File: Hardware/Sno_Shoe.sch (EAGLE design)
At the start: 39 parts, among them J1 QWIIC_RIGHT_ANGLE, J2 MOLEX_HDMI_208658-1051, U1 CH340E

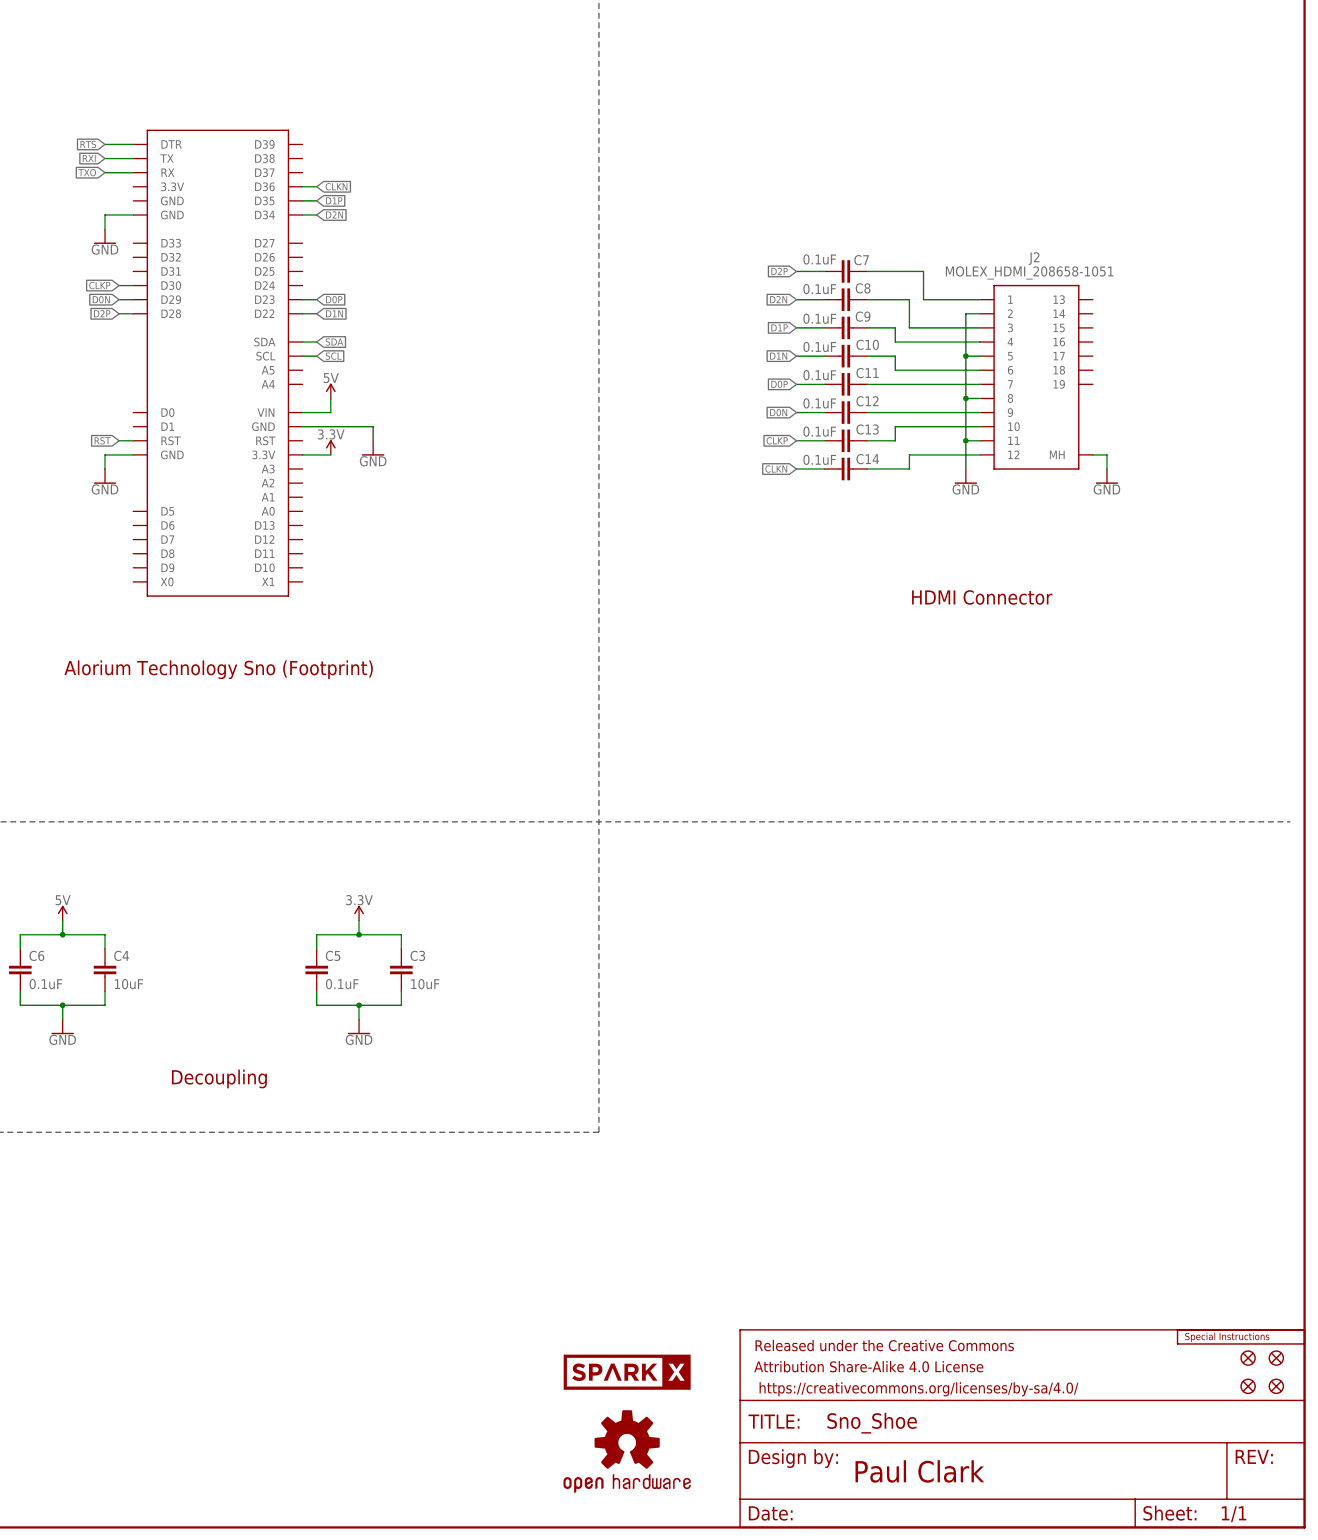
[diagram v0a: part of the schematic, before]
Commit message: Changed the HDMI connector footprint
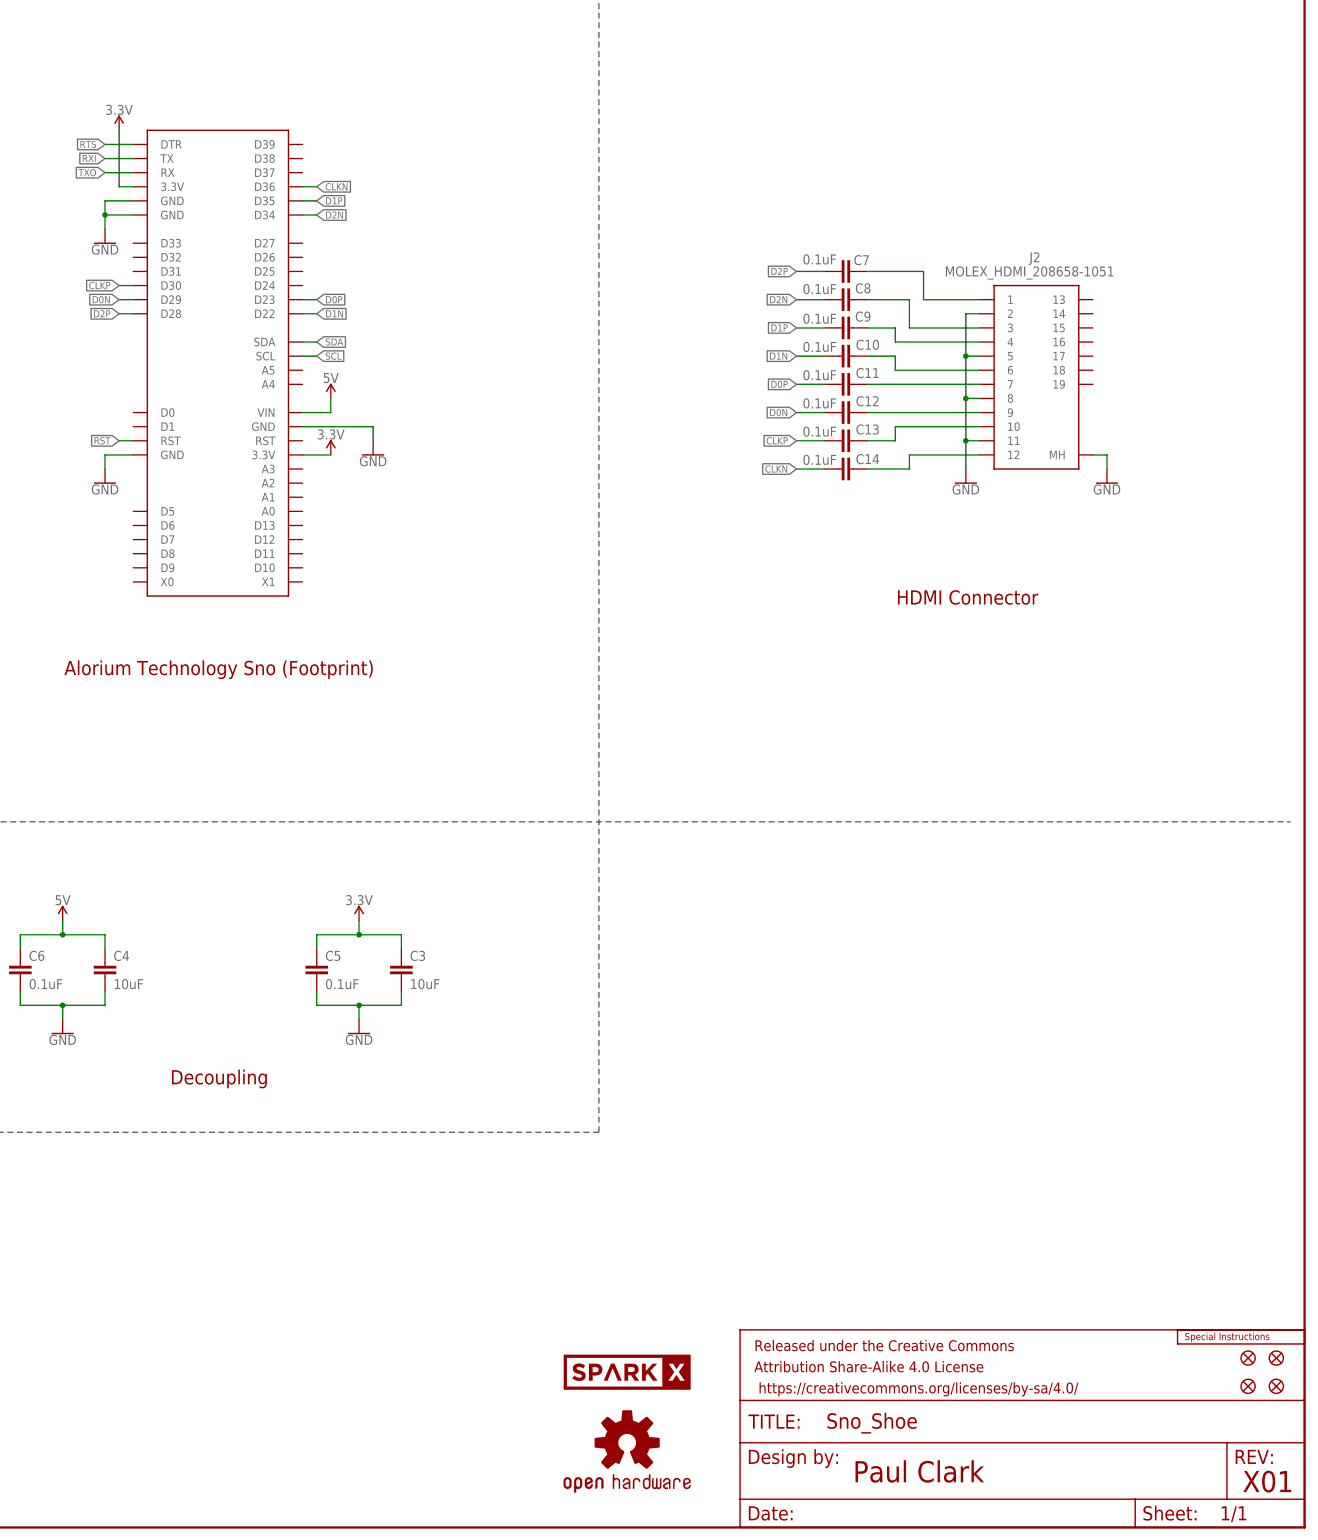
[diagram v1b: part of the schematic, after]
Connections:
- net 3.3V: now also U$1.3.3V@56
- net GND: now also U$1.GND@55
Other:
- note added: "X01"
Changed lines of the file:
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@@
 <class number="0" name="default" width="0" drill="0">
 </class>
-<class number="1" name="Power" width="0.4572" drill="0">
+<class number="1" name="Power" width="0.4064" drill="0">
 </class>
 </classes>
@@
 <part name="LOGO2" library="SparkFun-Aesthetics" deviceset="OSHW-LOGO" device="MINI" value="OSHW-LOGOMINI"/>
 <part name="SPARKX2" library="SparkX" deviceset="SPARKX-LOGO" device="4"/>
+<part name="SUPPLY1" library="SparkFun-PowerSymbols" deviceset="3.3V" device=""/>
 </parts>
 <sheets>
@@
 <wire x1="304.8" y1="71.12" x2="0" y2="71.12" width="0.2032" layer="97" style="longdash"/>
 <text x="236.474" y="154.686" size="2.54" layer="94" font="vector" align="center">Alorium Technology Sno (Footprint)</text>
-<text x="373.634" y="167.386" size="2.54" layer="94" font="vector" align="center">HDMI Connector</text>
+<text x="371.094" y="167.386" size="2.54" layer="94" font="vector" align="center">HDMI Connector</text>
 <text x="81.534" y="88.646" size="2.54" layer="94" font="vector" align="center">Reset Button</text>
 <text x="81.534" y="12.446" size="2.54" layer="94" font="vector" align="center">Qwiic I2C</text>
 <text x="236.474" y="81.026" size="2.54" layer="94" font="vector" align="center">Decoupling</text>
 <text x="350.52" y="8.128" size="3.81" layer="94">Paul Clark</text>
+<text x="420.624" y="6.35" size="3.81" layer="94">X01</text>
 </plain>
 <instances>
@@
 <instance part="LOGO2" gate="G$1" x="309.88" y="15.24" smashed="yes"/>
 <instance part="SPARKX2" gate="G$1" x="309.88" y="27.94" smashed="yes"/>
+<instance part="SUPPLY1" gate="G$1" x="218.44" y="251.46" smashed="yes">
+<attribute name="VALUE" x="218.44" y="254.254" size="1.778" layer="96" font="vector" align="bottom-center"/>
+</instance>
 </instances>
 <busses>
@@
 <wire x1="215.9" y1="236.22" x2="215.9" y2="233.68" width="0.1524" layer="91"/>
 <wire x1="220.98" y1="236.22" x2="215.9" y2="236.22" width="0.1524" layer="91"/>
+<pinref part="U$1" gate="G$1" pin="GND@55"/>
+<wire x1="220.98" y1="238.76" x2="215.9" y2="238.76" width="0.1524" layer="91"/>
+<wire x1="215.9" y1="238.76" x2="215.9" y2="236.22" width="0.1524" layer="91"/>
+<junction x="215.9" y="236.22"/>
 </segment>
 <segment>
@@
 <wire x1="251.46" y1="193.04" x2="256.54" y2="193.04" width="0.1524" layer="91"/>
 </segment>
+<segment>
+<pinref part="U$1" gate="G$1" pin="3.3V@56"/>
+<wire x1="220.98" y1="241.3" x2="218.44" y2="241.3" width="0.1524" layer="91"/>
+<pinref part="SUPPLY1" gate="G$1" pin="3.3V"/>
+<wire x1="218.44" y1="241.3" x2="218.44" y2="251.46" width="0.1524" layer="91"/>
+</segment>
 </net>
